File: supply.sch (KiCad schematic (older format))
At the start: 27 parts, among them J1 out, J2 2, J3 3, J4 1, J5 GND, J6 Conn_01x01_Female, J7 Conn_01x01_Female, J8 Conn_01x01_Female, J9 Conn_01x01_Female, U1 TPS61040DBV

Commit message: Add files via upload
updated
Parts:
- removed D2, D3: SB140-E3/54, Diode_THT:D_DO-41_SOD81_P7.62mm_Horizontal, symbol Device:D_Schottky
- removed U1: TPS61040DBV, Package_TO_SOT_SMD:SOT-23-5, symbol Regulator_Switching:TPS61040DBV
- added C10: 100nF, Capacitor_THT:C_Disc_D3.8mm_W2.6mm_P2.50mm, symbol Device:C
- added C8: 10nF, Capacitor_THT:C_Disc_D3.8mm_W2.6mm_P2.50mm, symbol Device:C
- added C9: 1nF, Capacitor_THT:C_Disc_D3.8mm_W2.6mm_P2.50mm, symbol Device:C
- added D2: 656320A304F, LED_THT:LED_Rectangular_W3.0mm_H2.0mm, symbol Device:LED
- added R5: 118K, Resistor_THT:R_Axial_DIN0207_L6.3mm_D2.5mm_P7.62mm_Horizontal, symbol Device:R
- added R6: 2.49K, Resistor_THT:R_Axial_DIN0207_L6.3mm_D2.5mm_P7.62mm_Horizontal, symbol Device:R
- added SW1: TE6-1A-DC-1-PB, Connector_PinHeader_2.00mm:PinHeader_2x01_P2.00mm_Vertical, symbol Switch:SW_SPST
- added U1: LM5157, Teensy:WQFN-16_EP_3.15x3.15_Pitch0.5mm, symbol Keyboard:LM5157
- BT1: value Battery 9V -> ACC-9VCLIP-233M
- C1: value 4.7 uF -> 4.7uF; footprint Capacitor_THT:C_Disc_D3.0mm_W1.6mm_P2.50mm -> Capacitor_THT:C_Disc_D3.8mm_W2.6mm_P2.50mm
- C2: value 1uF -> 100nF; footprint Capacitor_THT:C_Disc_D3.0mm_W1.6mm_P2.50mm -> Capacitor_THT:C_Disc_D3.8mm_W2.6mm_P2.50mm
- C3: value 4.7 uF -> 1nF; footprint Capacitor_THT:C_Disc_D3.0mm_W1.6mm_P2.50mm -> Capacitor_THT:C_Disc_D3.8mm_W2.6mm_P2.50mm
- C4: value 4.7 uF -> 68nF; footprint Capacitor_THT:C_Disc_D3.0mm_W1.6mm_P2.50mm -> Capacitor_THT:C_Disc_D3.8mm_W2.6mm_P2.50mm
- C5, C6: footprint Capacitor_THT:C_Disc_D3.0mm_W1.6mm_P2.50mm -> Capacitor_THT:C_Disc_D3.8mm_W2.6mm_P2.50mm
- C7: value 250pF -> 300pF; footprint Capacitor_THT:C_Disc_D3.0mm_W1.6mm_P2.50mm -> Capacitor_THT:C_Disc_D3.8mm_W2.6mm_P2.50mm
- D1: value SB140-E3/54 -> BAT42; footprint Diode_THT:D_DO-41_SOD81_P7.62mm_Horizontal -> Diode_THT:D_DO-35_SOD27_P7.62mm_Horizontal
- J1: value out -> MJ-3536
- L1: value 22 uH -> 2.7uH; footprint Resistor_THT:R_Axial_DIN0207_L6.3mm_D2.5mm_P7.62mm_Horizontal -> Inductor_THT:L_Axial_L9.5mm_D4.0mm_P12.70mm_Horizontal_Fastron_SMCC
- R1: value 1M -> 9.53K
- R2: value 27K -> 1.18K
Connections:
- wire segments 69 -> 114
- no-connect marks 7 -> 8
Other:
- note added: "pin2"
- note added: "pin3"
- moved on the sheet: BT1

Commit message: Add files via upload
Updated files.
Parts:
- added C11: 47uF, Capacitor_THT:C_Disc_D3.8mm_W2.6mm_P2.50mm, symbol Device:C
- added R7: 100, Resistor_THT:R_Axial_DIN0207_L6.3mm_D2.5mm_P7.62mm_Horizontal, symbol Device:R
- added RV1: R_POT_TRIM-10K, Connector_PinHeader_2.54mm:PinHeader_1x03_P2.54mm_Vertical, symbol Device:R_POT_TRIM
- added U2: NE5534, Package_DIP:DIP-8_W7.62mm_Socket, symbol Amplifier_Operational:NE5534
- U1: symbol Keyboard:LM5157 -> supply-rescue:LM5157-Keyboard
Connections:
- net labels added: VCC
- wire segments 114 -> 128
- no-connect marks 8 -> 12
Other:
- moved on the sheet: J1, J5
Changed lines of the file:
@@
 	4800 2900 5050 2900
 Wire Wire Line
-	4150 2900 4400 2900
-Wire Wire Line
-	4400 2500 4150 2500
+	4150 2900 4250 2900
 NoConn ~ 4400 2700
 NoConn ~ 4800 2700
@@
 Wire Wire Line
 	6550 2500 6550 2300
-Text Notes 2350 2850 0    50   ~ 0
+Text Notes 5650 1200 2    50   ~ 0
 Audio out
 Wire Wire Line
@@
 	6200 3350 6250 3350
 $Comp
-L Keyboard:LM5157 U1
+L supply-rescue:LM5157-Keyboard U1
 U 1 1 60D086D9
 P 5300 3950
@@
 Connection ~ 8500 5650
 Wire Wire Line
-	4150 2650 4150 2500
-Wire Wire Line
 	3550 3150 3550 2950
-Connection ~ 3550 2950
-Wire Wire Line
-	2950 2950 3550 2950
-Wire Wire Line
-	2950 2650 4150 2650
+Wire Wire Line
+	5050 1350 4250 1350
 $Comp
 L Connector:Conn_01x01_Female J1
 U 1 1 60CCEDFA
-P 2750 2650
-F 0 "J1" H 2642 2425 50  0000 C CNN
-F 1 "MJ-3536" H 2642 2516 50  0000 C CNN
-F 2 "MountingHole:MountingHole_2.2mm_M2_DIN965_Pad" H 2750 2650 50  0001 C CNN
-F 3 "~" H 2750 2650 50  0001 C CNN
-	1    2750 2650
-	-1   0    0    1
+P 5250 1350
+F 0 "J1" H 5142 1125 50  0000 C CNN
+F 1 "MJ-3536" H 5142 1216 50  0000 C CNN
+F 2 "MountingHole:MountingHole_2.2mm_M2_DIN965_Pad" H 5250 1350 50  0001 C CNN
+F 3 "~" H 5250 1350 50  0001 C CNN
+	1    5250 1350
+	1    0    0    -1
 $EndComp
 $Comp
 L Connector:Conn_01x01_Female J5
 U 1 1 60CCECCA
-P 2750 2950
-F 0 "J5" H 2642 2725 50  0000 C CNN
-F 1 "GND" H 2642 2816 50  0000 C CNN
-F 2 "MountingHole:MountingHole_2.2mm_M2_DIN965_Pad" H 2750 2950 50  0001 C CNN
-F 3 "~" H 2750 2950 50  0001 C CNN
-	1    2750 2950
-	-1   0    0    1
-$EndComp
-Text Notes 2500 3000 0    50   ~ 0
+P 5250 1050
+F 0 "J5" H 5142 825 50  0000 C CNN
+F 1 "GND" H 5142 916 50  0000 C CNN
+F 2 "MountingHole:MountingHole_2.2mm_M2_DIN965_Pad" H 5250 1050 50  0001 C CNN
+F 3 "~" H 5250 1050 50  0001 C CNN
+	1    5250 1050
+	1    0    0    -1
+$EndComp
+Text Notes 5500 1050 2    50   ~ 0
 pin2
-Text Notes 2500 2700 0    50   ~ 0
+Text Notes 5500 1350 2    50   ~ 0
 pin3
+$Comp
+L Amplifier_Operational:NE5534 U2
+U 1 1 60D1700B
+P 3400 1050
+F 0 "U2" H 3744 1096 50  0000 L CNN
+F 1 "NE5534" H 3744 1005 50  0000 L CNN
+F 2 "Package_DIP:DIP-8_W7.62mm_Socket" H 3450 1100 50  0001 C CNN
+F 3 "http://www.ti.com/lit/ds/symlink/ne5534.pdf" H 3450 1200 50  0001 C CNN
+	1    3400 1050
+	1    0    0    -1
+$EndComp
+Wire Wire Line
+	3100 950  2600 950
+Wire Wire Line
+	2600 950  2600 2500
+Wire Wire Line
+	2600 2500 4400 2500
+$Comp
+L Device:C C11
+U 1 1 60D41FD2
+P 3000 2750
+F 0 "C11" H 3115 2796 50  0000 L CNN
+F 1 "47uF" H 3050 2650 50  0000 L CNN
+F 2 "Capacitor_THT:C_Disc_D3.8mm_W2.6mm_P2.50mm" H 3038 2600 50  0001 C CNN
+F 3 "~" H 3000 2750 50  0001 C CNN
+	1    3000 2750
+	1    0    0    -1
+$EndComp
+$Comp
+L Device:R R7
+U 1 1 60D45884
+P 3000 2150
+F 0 "R7" H 3070 2196 50  0000 L CNN
+F 1 "100" H 3070 2105 50  0000 L CNN
+F 2 "Resistor_THT:R_Axial_DIN0207_L6.3mm_D2.5mm_P7.62mm_Horizontal" V 2930 2150 50  0001 C CNN
+F 3 "~" H 3000 2150 50  0001 C CNN
+	1    3000 2150
+	1    0    0    -1
+$EndComp
+Wire Wire Line
+	3550 2950 3300 2950
+Wire Wire Line
+	3000 2950 3000 2900
+Connection ~ 3550 2950
+Wire Wire Line
+	3000 2000 3000 1700
+Wire Wire Line
+	3000 1150 3100 1150
+$Comp
+L Device:R_POT_TRIM RV1
+U 1 1 60D5425C
+P 3800 1700
+F 0 "RV1" V 3685 1700 50  0000 C CNN
+F 1 "R_POT_TRIM-10K" V 3594 1700 50  0000 C CNN
+F 2 "Connector_PinHeader_2.54mm:PinHeader_1x03_P2.54mm_Vertical" H 3800 1700 50  0001 C CNN
+F 3 "~" H 3800 1700 50  0001 C CNN
+	1    3800 1700
+	0    -1   -1   0
+$EndComp
+Wire Wire Line
+	3300 1350 3300 2950
+Connection ~ 3300 2950
+Wire Wire Line
+	3300 2950 3000 2950
+Wire Wire Line
+	3000 2300 3000 2600
+Wire Wire Line
+	4250 1350 4250 2900
+Connection ~ 4250 2900
+Wire Wire Line
+	4250 2900 4400 2900
+Wire Wire Line
+	3650 1700 3000 1700
+Connection ~ 3000 1700
+Wire Wire Line
+	3000 1700 3000 1150
+Wire Wire Line
+	3800 1550 3800 1050
+Wire Wire Line
+	3800 1050 3700 1050
+Wire Wire Line
+	3800 1050 5050 1050
+Connection ~ 3800 1050
+NoConn ~ 3950 1700
+Text GLabel 3900 3800 1    50   Input ~ 0
+VCC
+Text GLabel 3300 750  1    50   Input ~ 0
+VCC
+NoConn ~ 3500 1350
+NoConn ~ 3400 1350
+NoConn ~ 3400 750
 $EndSCHEMATC

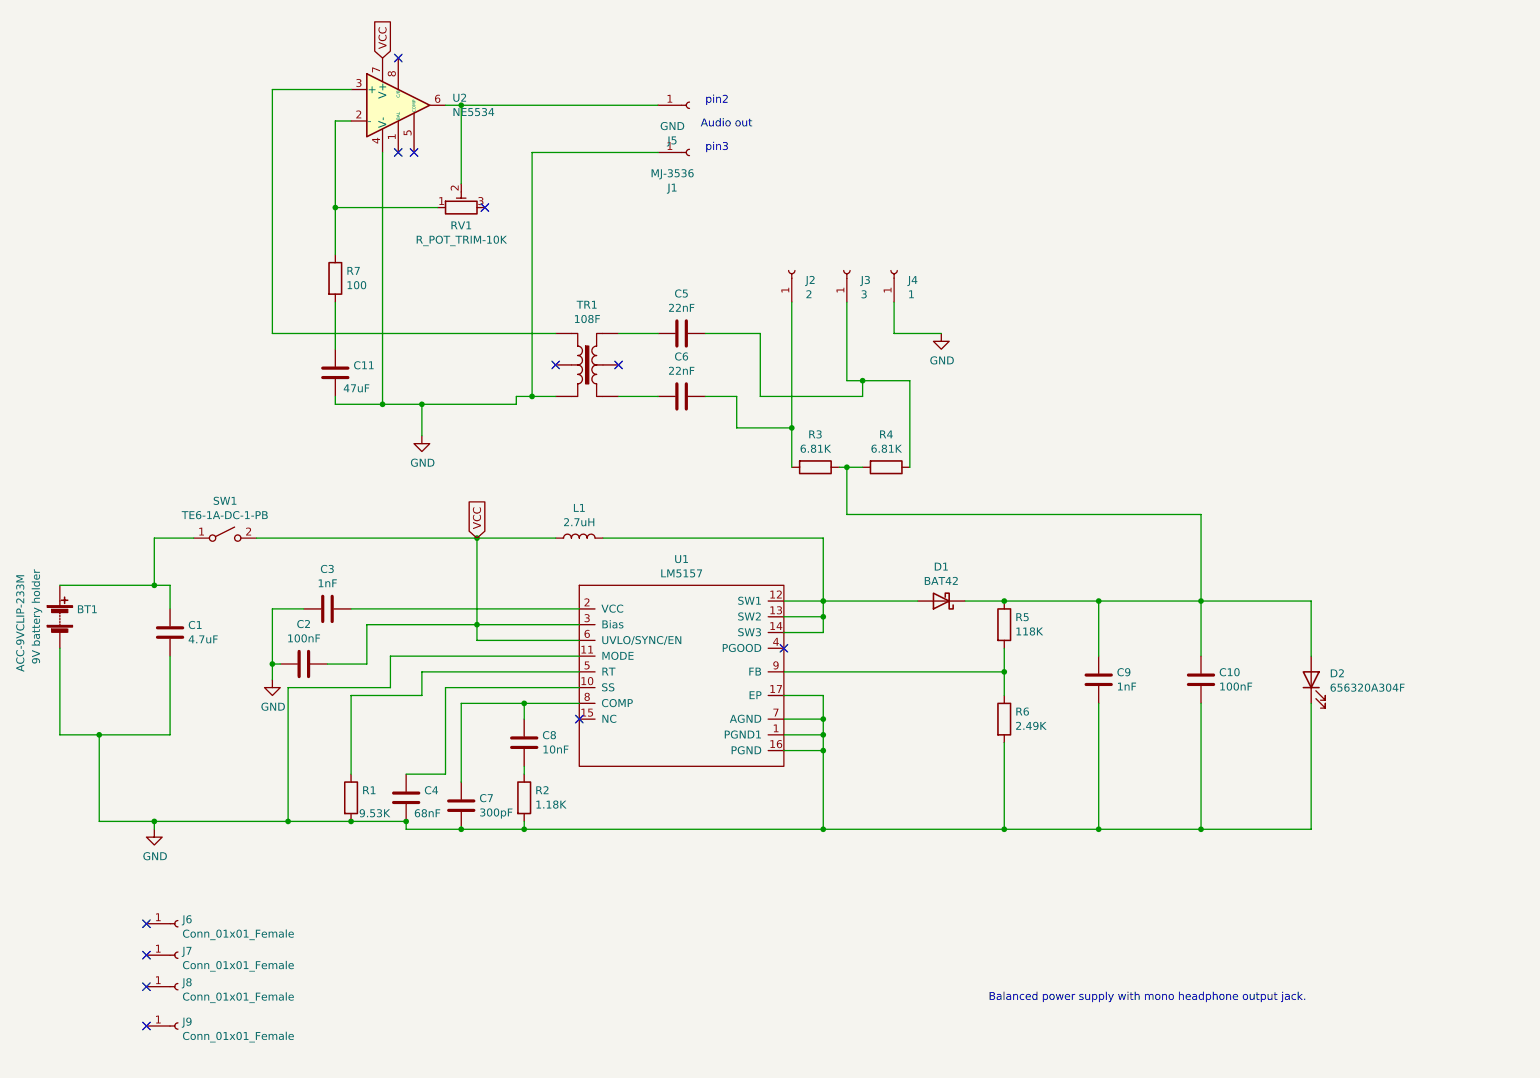
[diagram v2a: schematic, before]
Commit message: Add files via upload
update, added correct diode and PCT fuse.
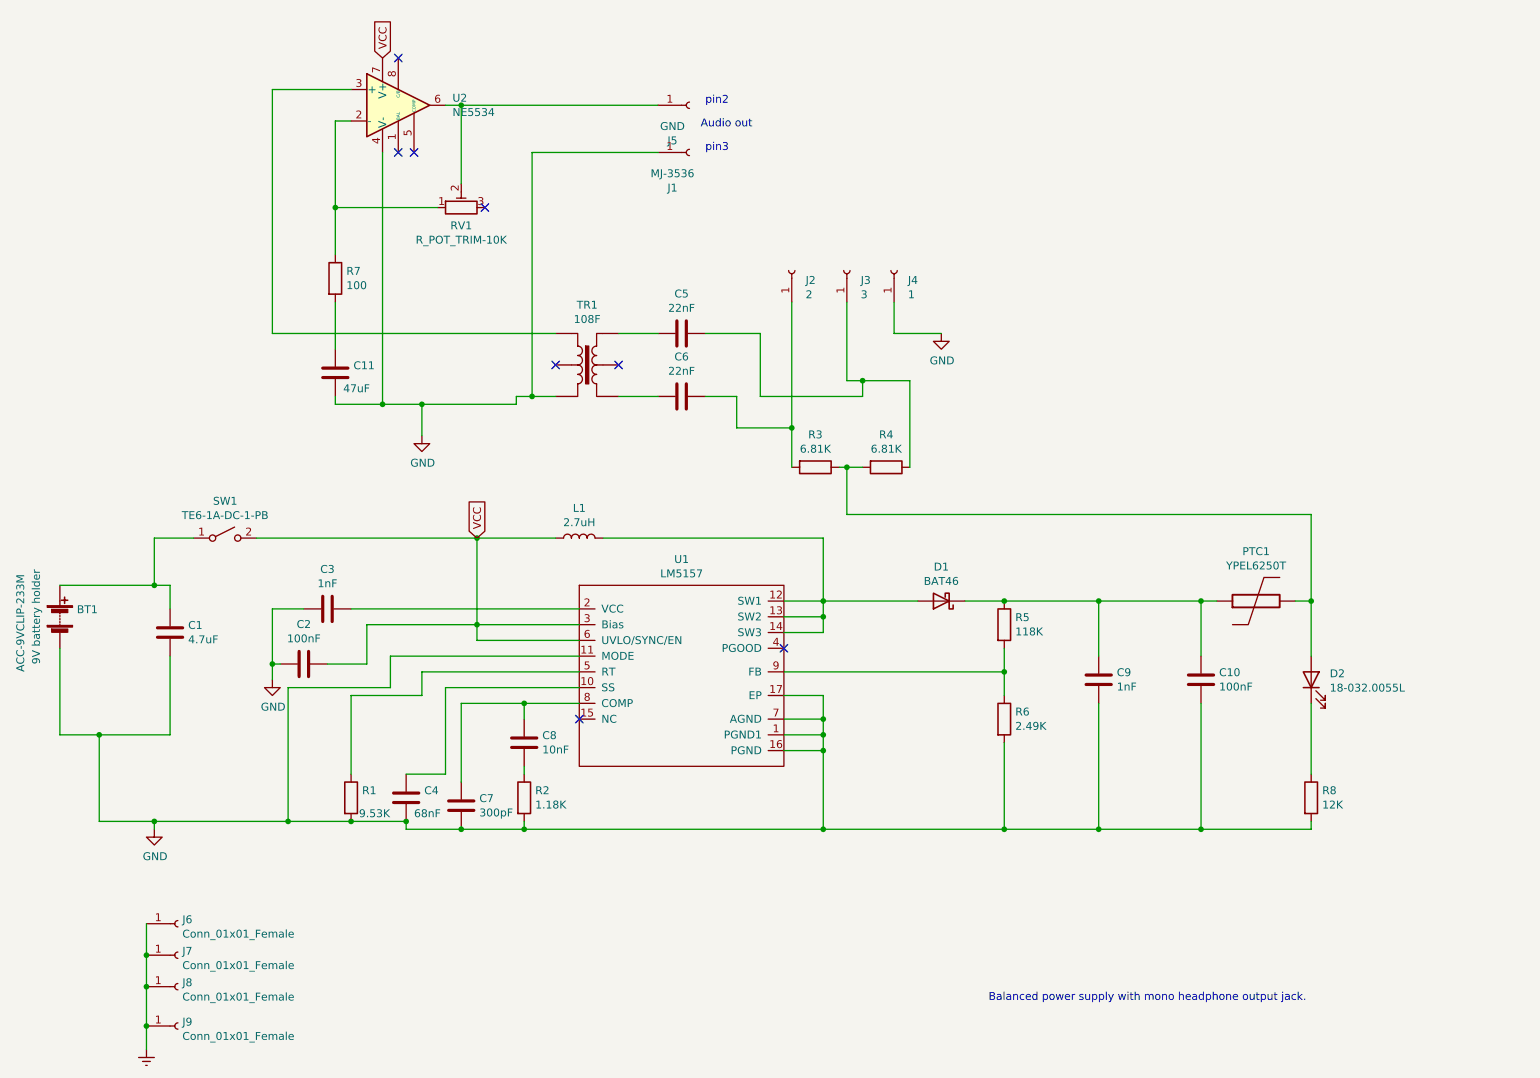
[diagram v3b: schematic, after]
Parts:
- added PTC1: YPEL6250T, Resistor_THT:R_Axial_DIN0204_L3.6mm_D1.6mm_P5.08mm_Horizontal, symbol keyboard:PTC
- added R8: 12K, Resistor_THT:R_Axial_DIN0204_L3.6mm_D1.6mm_P7.62mm_Horizontal, symbol Device:R
- D1: value BAT42 -> BAT46
- D2: value 656320A304F -> 18-032.0055L; footprint LED_THT:LED_Rectangular_W3.0mm_H2.0mm -> LED_THT:LED_D2.0mm_W4.8mm_H2.5mm_FlatTop
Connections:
- net GND: now also R8.2; no longer D2.1 (K)
- net Earth: now reaches J6.1 (Pin_1)
- net Earth: now also J7.1 (Pin_1), J8.1 (Pin_1), J9.1 (Pin_1)
- net at C10.2, C9.2, D1.1 (K)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: now also PTC1.1; no longer D2.2 (A), R3.1, R4.2
- new net: D2.2 (A), PTC1.2, R3.1, R4.2
- new net: D2.1 (K), R8.1
- no-connect marks 12 -> 8
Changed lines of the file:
@@
 	1    0    0    -1
 $EndComp
-NoConn ~ 1800 6250
-NoConn ~ 1800 6450
-NoConn ~ 1800 6650
-NoConn ~ 1800 6900
 Wire Wire Line
 	6200 3350 6250 3350
@@
 P 6850 4200
 F 0 "D1" H 6850 3983 50  0000 C CNN
-F 1 "BAT42" H 6850 4074 50  0000 C CNN
+F 1 "BAT46" H 6850 4074 50  0000 C CNN
 F 2 "Diode_THT:D_DO-35_SOD27_P7.62mm_Horizontal" H 6850 4200 50  0001 C CNN
 F 3 "~" H 6850 4200 50  0001 C CNN
@@
 Connection ~ 7850 4200
 Wire Wire Line
-	8500 4200 8500 3650
-Wire Wire Line
-	8500 3650 6250 3650
-Wire Wire Line
 	6250 3650 6250 3350
 Connection ~ 8500 4200
@@
 Wire Wire Line
 	2100 3800 1850 3800
-$Comp
-L Device:LED D2
-U 1 1 60D7E3BE
-P 9200 4700
-F 0 "D2" V 9239 4582 50  0000 R CNN
-F 1 "656320A304F" V 9148 4582 50  0000 R CNN
-F 2 "LED_THT:LED_Rectangular_W3.0mm_H2.0mm" H 9200 4700 50  0001 C CNN
-F 3 "~" H 9200 4700 50  0001 C CNN
-	1    9200 4700
-	0    -1   -1   0
-$EndComp
-Wire Wire Line
-	8500 4200 9200 4200
-Wire Wire Line
-	9200 4200 9200 4550
-Wire Wire Line
-	9200 4850 9200 5650
+Wire Wire Line
+	8500 4200 8600 4200
 Wire Wire Line
 	9200 5650 8500 5650
@@
 NoConn ~ 3400 1350
 NoConn ~ 3400 750
+$Comp
+L keyboard:PTC PTC1
+U 1 1 60D2EB90
+P 8850 4200
+F 0 "PTC1" H 8850 4515 50  0000 C CNN
+F 1 "YPEL6250T" H 8850 4424 50  0000 C CNN
+F 2 "Resistor_THT:R_Axial_DIN0204_L3.6mm_D1.6mm_P5.08mm_Horizontal" V 8850 4200 60  0001 C CNN
+F 3 "" V 8850 4200 60  0000 C CNN
+	1    8850 4200
+	1    0    0    -1
+$EndComp
+Wire Wire Line
+	9100 4200 9200 4200
+$Comp
+L Device:R R8
+U 1 1 60D30BFB
+P 9200 5450
+F 0 "R8" H 9270 5496 50  0000 L CNN
+F 1 "12K" H 9270 5405 50  0000 L CNN
+F 2 "Resistor_THT:R_Axial_DIN0204_L3.6mm_D1.6mm_P7.62mm_Horizontal" V 9130 5450 50  0001 C CNN
+F 3 "~" H 9200 5450 50  0001 C CNN
+	1    9200 5450
+	1    0    0    -1
+$EndComp
+$Comp
+L Device:LED D2
+U 1 1 60D31DED
+P 9200 4700
+F 0 "D2" V 9239 4582 50  0000 R CNN
+F 1 "18-032.0055L" V 9148 4582 50  0000 R CNN
+F 2 "LED_THT:LED_D2.0mm_W4.8mm_H2.5mm_FlatTop" H 9200 4700 50  0001 C CNN
+F 3 "~" H 9200 4700 50  0001 C CNN
+	1    9200 4700
+	0    -1   -1   0
+$EndComp
+Wire Wire Line
+	9200 4200 9200 3650
+Wire Wire Line
+	6250 3650 9200 3650
+Connection ~ 9200 4200
+Wire Wire Line
+	9200 5600 9200 5650
+Wire Wire Line
+	9200 4200 9200 4550
+Wire Wire Line
+	9200 4850 9200 5300
+Wire Wire Line
+	1800 6250 1800 6450
+Wire Wire Line
+	1800 6450 1800 6650
+Connection ~ 1800 6450
+Wire Wire Line
+	1800 6650 1800 6900
+Connection ~ 1800 6650
+$Comp
+L power:Earth #PWR0101
+U 1 1 60D710DF
+P 1800 7050
+F 0 "#PWR0101" H 1800 6800 50  0001 C CNN
+F 1 "Earth" H 1800 6900 50  0001 C CNN
+F 2 "" H 1800 7050 50  0001 C CNN
+F 3 "~" H 1800 7050 50  0001 C CNN
+	1    1800 7050
+	1    0    0    -1
+$EndComp
+Wire Wire Line
+	1800 7050 1800 6900
+Connection ~ 1800 6900
 $EndSCHEMATC
